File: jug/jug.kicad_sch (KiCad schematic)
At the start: 96 parts, among them J1 USB_A, J2 USB_A, U1 RP2040_Pro_Micro, U2 RP2040_Pro_Micro

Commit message: finished pcb with RP2040 Pro Micro
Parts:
- removed D24, D25, D27, D28, D29, D30, D31, D32, D33, D34, D35, D36, D37, D38, D39, D40, D41, D42, D43, D44, D45, D46, D47: D, ScottoKeebs_Components:Double_Sided_Diode_DO-35, symbol Device:D
- removed J2: USB_A, Connector_USB:USB_A_Molex_67643_Horizontal, symbol Connector:USB_A
- removed S24, S25, S26, S27, S28, S29, S30, S31, S32, S33, S34, S35, S36, S37, S38, S39, S40, S41, S42, S43, S44: Keyswitch, ScottoKeebs_Hotswap:Hotswap_MX_Plated_1.00u, symbol ScottoKeebs:Placeholder_Keyswitch
- removed S45, S46: Keyswitch, ScottoKeebs_Hotswap:Hotswap_MX_Plated_1.50u_90deg, symbol ScottoKeebs:Placeholder_Keyswitch
- removed U1, U2: RP2040_Pro_Micro, ScottoKeebs_MCU:RP2040_Pro_Micro, symbol ScottoKeebs:MCU_RP2040_Pro_Micro
- added D24, D25, D26, D27: LED, LED_SMD:LED_1206_3216Metric_Pad1.42x1.75mm_HandSolder, symbol Device:LED
- added JP1, JP2, JP3, JP4, JP5, JP6, JP7, JP8: SolderJumper_2_Open, Jumper:SolderJumper-2_P1.3mm_Open_TrianglePad1.0x1.5mm, symbol Jumper:SolderJumper_2_Open
- added R1, R2, R3, R4: R, Resistor_SMD:R_1206_3216Metric_Pad1.30x1.75mm_HandSolder, symbol Device:R
- added U2: Arduino_Pro_Micro, keyboard_reversible:ProMicro_flipped, symbol ScottoKeebs:MCU_Arduino_Pro_Micro
- S10, S11, S12, S13, S14, S15, S16, S17, S18, S19, S2, S20, S21, S3, S4, S5, S6, S7, S8, S9: footprint ScottoKeebs_Hotswap:Hotswap_MX_Plated_1.00u -> ScottoKeebs_Hotswap:Hotswap_MX_Plated_1.00u_Reversible
- S22, S23: footprint ScottoKeebs_Hotswap:Hotswap_MX_Plated_1.50u_90deg -> ScottoKeebs_Hotswap:Hotswap_MX_Plated_1.50u_90deg_Reversible
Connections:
- net +5V: now also JP5.1 (A), JP7.1 (A), U2.24 (RAW); no longer J1.1 (VBUS)
- net COL0L: now also U2.18 (A1/PF6)
- net COL1L: now also U2.17 (A0/PF7)
- net COL2L: now also U2.16 (15/PB1)
- net COL3L: now also U2.15 (14/PB3)
- net COL4L: now also U2.14 (16/PB2)
- net COL5L: now also U2.13 (10/PB6)
- net GND: now also JP6.2 (B), JP8.2 (B), R1.2, R2.2, R3.2, R4.2, U2.23 (GND), U2.3 (GND), U2.4 (GND); no longer J1.4 (GND)
- net INTERCONNECT_A: now also JP1.1 (A), JP3.1 (A), U2.20 (A3/PF4); no longer J1.2 (D-)
- net INTERCONNECT_B: now also JP2.2 (B), JP4.2 (B), U2.19 (A2/PF5); no longer J1.3 (D+)
- net ROW0L: now also U2.6 (3/PD0)
- net ROW1L: now also U2.7 (4/PD4)
- net ROW2L: now also U2.8 (5/PC6)
- net ROW3L: now also U2.9 (6/PD7)
- new net: J1.4 (GND), JP5.2 (B), JP8.1 (A)
- new net: D26.1 (K), R3.1
- new net: J1.2 (D-), JP1.2 (B), JP4.1 (A)
- new net: J1.3 (D+), JP2.1 (A), JP3.2 (B)
- new net: D27.1 (K), R4.1
- new net: D24.1 (K), R1.1
- new net: J1.1 (VBUS), JP6.1 (A), JP7.2 (B)
- new net: D25.1 (K), R2.1
- new net LED0: D24.2 (A), D26.2 (A), U2.11 (8/PB4)
- new net LED1: D25.2 (A), D27.2 (A), U2.12 (9/PB5)
- no-connect marks 4 -> 6
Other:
- moved on the sheet: D1, D10, D11, D12, D13, D14, D15, D16, D17, D18, D19, D2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

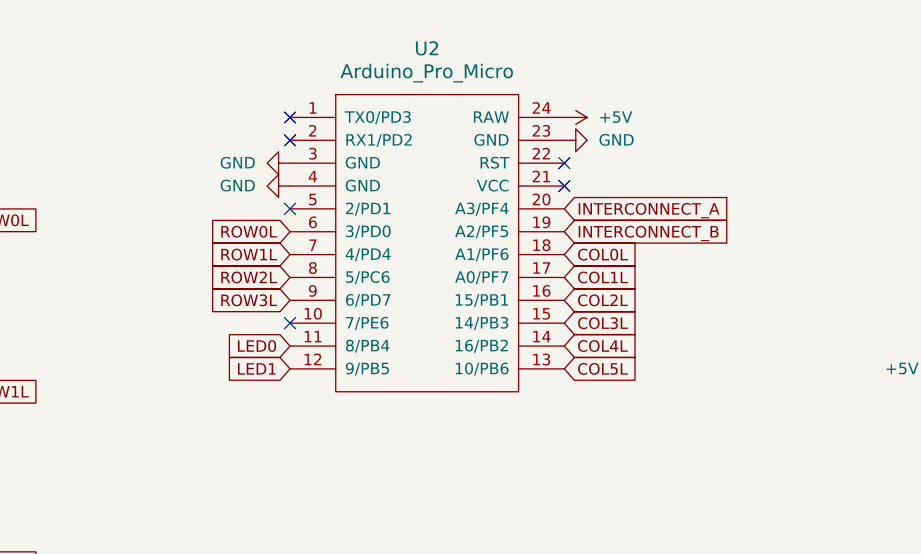
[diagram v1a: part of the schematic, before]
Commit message: changed mcu to rp2040 zero with reversible footprint
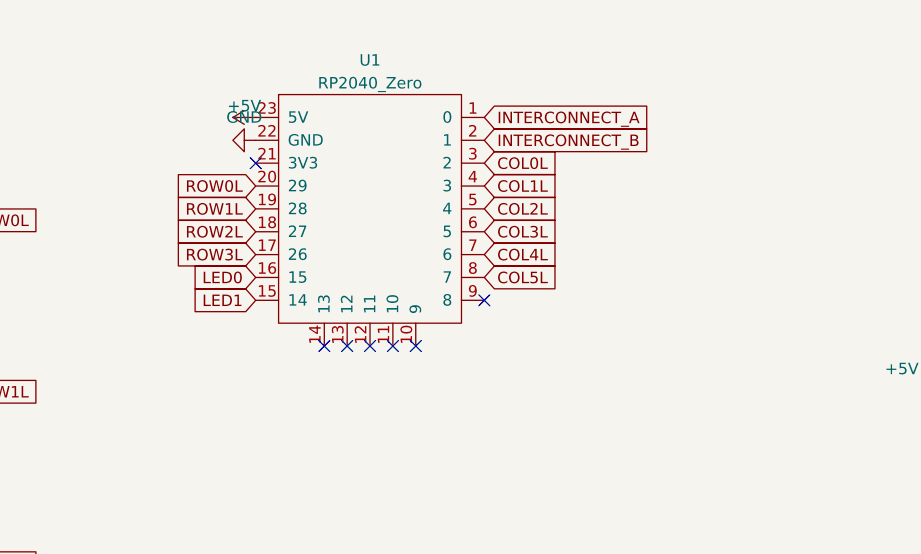
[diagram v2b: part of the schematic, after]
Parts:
- removed U2: Arduino_Pro_Micro, keyboard_reversible:ProMicro_flipped, symbol ScottoKeebs:MCU_Arduino_Pro_Micro
- added U1: RP2040_Zero, ScottoKeebs_MCU:RP2040_Zero_Reversible, symbol ScottoKeebs:MCU_RP2040_Zero
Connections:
- net +5V: now also U1.23 (5V)
- net COL0L: now also U1.3 (2)
- net COL1L: now also U1.4 (3)
- net COL2L: now also U1.5 (4)
- net COL3L: now also U1.6 (5)
- net COL4L: now also U1.7 (6)
- net COL5L: now also U1.8 (7)
- net GND: now also U1.22 (GND)
- net INTERCONNECT_A: now also U1.1 (0)
- net INTERCONNECT_B: now also U1.2 (1)
- net LED0: now also U1.16 (15)
- net LED1: now also U1.15 (14)
- net ROW0L: now also U1.20 (29)
- net ROW1L: now also U1.19 (28)
- net ROW2L: now also U1.18 (27)
- net ROW3L: now also U1.17 (26)
- no-connect marks 6 -> 7

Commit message: finished pcb
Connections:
- net LED0: now also D25.2 (A); no longer D26.2 (A)
- net LED1: now also D26.2 (A); no longer D25.2 (A)
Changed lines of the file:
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@@
+		)
+	)
+	(global_label "LED1"
+		(shape input)
+		(at 172.72 82.55 180)
+		(fields_autoplaced yes)
+		(effects
+			(font
+				(size 1.27 1.27)
+			)
+			(justify right)
+		)
+		(property "Intersheetrefs" "${INTERSHEET_REFS}"
+			(at 165.0782 82.55 0)
+			(effects
+				(font
+					(size 1.27 1.27)
+				)
+				(justify right)
+				(hide yes)
+			)
 		)
 	)
@@
 		)
 	)
-	(global_label "LED1"
+	(global_label "ROW3L"
+		(shape input)
+		(at 97.79 95.25 0)
+		(fields_autoplaced yes)
+		(effects
+			(font
+				(size 1.27 1.27)
+			)
+			(justify left)
+		)
+		(property "Intersheetrefs" "${INTERSHEET_REFS}"
+			(at 107.0647 95.25 0)
+			(effects
+				(font
+					(size 1.27 1.27)
+				)
+				(justify left)
+				(hide yes)
+			)
+		)
+	)
+	(global_label "INTERCONNECT_A"
+		(shape input)
+		(at 144.78 25.4 0)
+		(fields_autoplaced yes)
+		(effects
+			(font
+				(size 1.27 1.27)
+			)
+			(justify left)
+		)
+		(property "Intersheetrefs" "${INTERSHEET_REFS}"
+			(at 163.7914 25.4 0)
+			(effects
+				(font
+					(size 1.27 1.27)
+				)
+				(justify left)
+				(hide yes)
+			)
+		)
+	)
+	(global_label "ROW2L"
+		(shape input)
+		(at 86.36 74.93 0)
+		(fields_autoplaced yes)
+		(effects
+			(font
+				(size 1.27 1.27)
+			)
+			(justify left)
+		)
+		(property "Intersheetrefs" "${INTERSHEET_REFS}"
+			(at 95.6347 74.93 0)
+			(effects
+				(font
+					(size 1.27 1.27)
+				)
+				(justify left)
+				(hide yes)
+			)
+		)
+	)
+	(global_label "INTERCONNECT_B"
+		(shape input)
+		(at 273.05 34.29 0)
+		(fields_autoplaced yes)
+		(effects
+			(font
+				(size 1.27 1.27)
+			)
+			(justify left)
+		)
+		(property "Intersheetrefs" "${INTERSHEET_REFS}"
+			(at 292.2428 34.29 0)
+			(effects
+				(font
+					(size 1.27 1.27)
+				)
+				(justify left)
+				(hide yes)
+			)
+		)
+	)
+	(global_label "ROW2L"
+		(shape input)
+		(at 119.38 38.1 180)
+		(fields_autoplaced yes)
+		(effects
+			(font
+				(size 1.27 1.27)
+			)
+			(justify right)
+		)
+		(property "Intersheetrefs" "${INTERSHEET_REFS}"
+			(at 110.1053 38.1 0)
+			(effects
+				(font
+					(size 1.27 1.27)
+				)
+				(justify right)
+				(hide yes)
+			)
+		)
+	)
+	(global_label "INTERCONNECT_A"
+		(shape input)
+		(at 234.95 34.29 180)
+		(fields_autoplaced yes)
+		(effects
+			(font
+				(size 1.27 1.27)
+			)
+			(justify right)
+		)
+		(property "Intersheetrefs" "${INTERSHEET_REFS}"
+			(at 215.9386 34.29 0)
+			(effects
+				(font
+					(size 1.27 1.27)
+				)
+				(justify right)
+				(hide yes)
+			)
+		)
+	)
+	(global_label "LED0"
+		(shape input)
+		(at 119.38 43.18 180)
+		(fields_autoplaced yes)
+		(effects
+			(font
+				(size 1.27 1.27)
+			)
+			(justify right)
+		)
+		(property "Intersheetrefs" "${INTERSHEET_REFS}"
+			(at 111.7382 43.18 0)
+			(effects
+				(font
+					(size 1.27 1.27)
+				)
+				(justify right)
+				(hide yes)
+			)
+		)
+	)
+	(global_label "LED0"
 		(shape input)
 		(at 135.89 93.98 180)
@@
 			(effects
 				(font
-					(size 1.27 1.27)
-				)
-				(justify right)
-				(hide yes)
-			)
-		)
-	)
-	(global_label "ROW3L"
-		(shape input)
-		(at 97.79 95.25 0)
-		(fields_autoplaced yes)
-		(effects
-			(font
-				(size 1.27 1.27)
-			)
-			(justify left)
-		)
-		(property "Intersheetrefs" "${INTERSHEET_REFS}"
-			(at 107.0647 95.25 0)
-			(effects
-				(font
-					(size 1.27 1.27)
-				)
-				(justify left)
-				(hide yes)
-			)
-		)
-	)
-	(global_label "INTERCONNECT_A"
-		(shape input)
-		(at 144.78 25.4 0)
-		(fields_autoplaced yes)
-		(effects
-			(font
-				(size 1.27 1.27)
-			)
-			(justify left)
-		)
-		(property "Intersheetrefs" "${INTERSHEET_REFS}"
-			(at 163.7914 25.4 0)
-			(effects
-				(font
-					(size 1.27 1.27)
-				)
-				(justify left)
-				(hide yes)
-			)
-		)
-	)
-	(global_label "ROW2L"
-		(shape input)
-		(at 86.36 74.93 0)
-		(fields_autoplaced yes)
-		(effects
-			(font
-				(size 1.27 1.27)
-			)
-			(justify left)
-		)
-		(property "Intersheetrefs" "${INTERSHEET_REFS}"
-			(at 95.6347 74.93 0)
-			(effects
-				(font
-					(size 1.27 1.27)
-				)
-				(justify left)
-				(hide yes)
-			)
-		)
-	)
-	(global_label "LED0"
-		(shape input)
-		(at 172.72 82.55 180)
-		(fields_autoplaced yes)
-		(effects
-			(font
-				(size 1.27 1.27)
-			)
-			(justify right)
-		)
-		(property "Intersheetrefs" "${INTERSHEET_REFS}"
-			(at 165.0782 82.55 0)
-			(effects
-				(font
-					(size 1.27 1.27)
-				)
-				(justify right)
-				(hide yes)
-			)
-		)
-	)
-	(global_label "INTERCONNECT_B"
-		(shape input)
-		(at 273.05 34.29 0)
-		(fields_autoplaced yes)
-		(effects
-			(font
-				(size 1.27 1.27)
-			)
-			(justify left)
-		)
-		(property "Intersheetrefs" "${INTERSHEET_REFS}"
-			(at 292.2428 34.29 0)
-			(effects
-				(font
-					(size 1.27 1.27)
-				)
-				(justify left)
-				(hide yes)
-			)
-		)
-	)
-	(global_label "ROW2L"
-		(shape input)
-		(at 119.38 38.1 180)
-		(fields_autoplaced yes)
-		(effects
-			(font
-				(size 1.27 1.27)
-			)
-			(justify right)
-		)
-		(property "Intersheetrefs" "${INTERSHEET_REFS}"
-			(at 110.1053 38.1 0)
-			(effects
-				(font
-					(size 1.27 1.27)
-				)
-				(justify right)
-				(hide yes)
-			)
-		)
-	)
-	(global_label "INTERCONNECT_A"
-		(shape input)
-		(at 234.95 34.29 180)
-		(fields_autoplaced yes)
-		(effects
-			(font
-				(size 1.27 1.27)
-			)
-			(justify right)
-		)
-		(property "Intersheetrefs" "${INTERSHEET_REFS}"
-			(at 215.9386 34.29 0)
-			(effects
-				(font
-					(size 1.27 1.27)
-				)
-				(justify right)
-				(hide yes)
-			)
-		)
-	)
-	(global_label "LED0"
-		(shape input)
-		(at 119.38 43.18 180)
-		(fields_autoplaced yes)
-		(effects
-			(font
-				(size 1.27 1.27)
-			)
-			(justify right)
-		)
-		(property "Intersheetrefs" "${INTERSHEET_REFS}"
-			(at 111.7382 43.18 0)
-			(effects
-				(font
